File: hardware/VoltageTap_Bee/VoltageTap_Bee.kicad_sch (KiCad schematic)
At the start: 50 parts, among them J101 Conn_02x05_Odd_Even, J102 VT, J106 uart, Q101 TSM2328CX, SW101 SW_Push, U101 XMSM0G3507SDGS28R, U102 ISOM8110DFS, U103 ISO1044BD, U104 TLP176AM, U105 AP7384-50SA, U106 STISO620

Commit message: c&p master
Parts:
- removed CR?: ESD2CAN36DBZRQ1, Package_TO_SOT_SMD:TSOT-23_HandSoldering, symbol zzLocalLibrary:ESD2CAN36DBZRQ1
- removed D101, D102: LED, LED_SMD:LED_0603_1608Metric, symbol Device:LED
- removed D?: ES1D, Diode_SMD:D_SMA, symbol Device:D_Schottky_Small
- removed FL?: Choke_CommonMode_FerriteCore_1243, Inductor_SMD:L_CommonModeChoke_Coilcraft_1812CAN, symbol Filter:Choke_CommonMode_FerriteCore_1243
- removed J?: Conn_01x04_Pin, Connector_PinHeader_2.54mm:PinHeader_1x04_P2.54mm_Vertical, symbol Connector:Conn_01x04_Pin
- removed J?: HRLV, Connector_Molex:Molex_Micro-Fit_3.0_43045-0600_2x03_P3.00mm_Horizontal, symbol Connector_Generic:Conn_02x03_Top_Bottom
- removed Q101: TSM2328CX, Package_TO_SOT_SMD:SOT-23-3, symbol Transistor_FET:Q_NMOS_GSD
- removed R105, R111: 750, Resistor_SMD:R_1206_3216Metric_Pad1.30x1.75mm_HandSolder, symbol Device:R_US
- removed R107: 88.7k, Resistor_SMD:R_0805_2012Metric_Pad1.20x1.40mm_HandSolder, symbol Device:R_Small_US
- removed R112, R113, R114: 750, Resistor_SMD:R_1206_3216Metric_Pad1.30x1.75mm_HandSolder, symbol Device:R_Small_US
- removed U102: ISOM8110DFS, zzLocalLibraries-Footprints:ISOM811_SOIC-4_DFG, symbol zzLocalLibrary:ISOM811_0_3
- removed U103: ISO1044BD, Package_SO:SOIC-8_5.3x5.3mm_P1.27mm, symbol Interface_CAN_LIN:ISO1044BD
- removed U105: AP7384-50SA, Package_TO_SOT_SMD:SOT-23, symbol Regulator_Linear:AP7384-50SA
- removed U106: STISO620, Package_SO:SOIC-8_7.5x5.85mm_P1.27mm, symbol zzLocalLibrary:STISO621
- added C106: 22u, Capacitor_SMD:C_0805_2012Metric_Pad1.18x1.45mm_HandSolder, symbol Device:C_Small
- added C107, C109: 100n, Capacitor_SMD:C_0603_1608Metric_Pad1.08x0.95mm_HandSolder, symbol Device:C_Small
- added C112: 1u, Capacitor_SMD:C_0603_1608Metric_Pad1.08x0.95mm_HandSolder, symbol Device:C_Small
- added CR101: ESD2CAN36DBZRQ1, Package_TO_SOT_SMD:TSOT-23_HandSoldering, symbol zzLocalLibrary:ESD2CAN36DBZRQ1
- added D101: ES1D, Diode_SMD:D_SMA, symbol Device:D_Schottky_Small
- added D102: green, LED_SMD:LED_0805_2012Metric_Pad1.15x1.40mm_HandSolder, symbol Device:LED_Small
- added D104: yellow, LED_SMD:LED_0805_2012Metric_Pad1.15x1.40mm_HandSolder, symbol Device:LED_Small
- added FL101: Choke_CommonMode_FerriteCore_1243, Inductor_SMD:L_CommonModeChoke_Coilcraft_1812CAN, symbol Filter:Choke_CommonMode_FerriteCore_1243
- added J102: HRLV daisy A, Connector_Molex:Molex_Micro-Fit_3.0_43045-0600_2x03_P3.00mm_Horizontal, symbol Connector_Generic:Conn_02x03_Top_Bottom
- added J103: HRLV daisy B, Connector_Molex:Molex_Micro-Fit_3.0_43045-0600_2x03_P3.00mm_Horizontal, symbol Connector_Generic:Conn_02x03_Top_Bottom
- added R105: 10k, Resistor_SMD:R_0805_2012Metric_Pad1.20x1.40mm_HandSolder, symbol Device:R_Small_US
- added R109: 3.32k, Resistor_SMD:R_0805_2012Metric_Pad1.20x1.40mm_HandSolder, symbol Device:R_Small_US
- added U101: TPSM33606S5QRDNRQ1, zzLocalLibraries-Footprints:RDN0011A_TEX, symbol zzLocalLibrary:TPSM33606S5QRDNRQ1
- added U103: ISOM8110DFS, zzLocalLibraries-Footprints:ISOM811_SOIC-4_DFG, symbol zzLocalLibrary:ISOM811_0_3
- added U104: NCP163ASN330T1G, Package_TO_SOT_SMD:SOT-23-5_HandSoldering, symbol Regulator_Linear:NCP163ASN330T1G
- added U105: XISO6441DWR, zzLocalLibraries-Footprints:SOIC16_DW_TEX-M, symbol zzLocalLibrary:XISO6441DWR
- added U106: MCP2542FDxMF, Package_SO:SOIC-8_3.9x4.9mm_P1.27mm, symbol Interface_CAN_LIN:MCP2542FDxMF
- C101: value 100n -> 220n; footprint Capacitor_SMD:C_0603_1608Metric_Pad1.08x0.95mm_HandSolder -> Capacitor_SMD:C_0805_2012Metric_Pad1.18x1.45mm_HandSolder; Mouser Part Number 710-885012206095 -> (none); mouser https://www.mouser.com/ProductDetail/Wurth-Elektronik/88501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 -> https://www.mouser.com/ProductDetail/Samsung-Electro-Mechan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; specs 100nF, 10%, 50V, X7R, -55C, +125C -> 100VDC, X7R, 10%, -55C, +125C, 220nF; unit x1 0.10 -> (none); unit x10 0.029 -> 0.054; unit x100 0.017 -> (none); unit x50 0.02 -> (none)
- C102: value 100n -> 1u; Mouser Part Number 710-885012206095 -> (none); mouser https://www.mouser.com/ProductDetail/Wurth-Elektronik/88501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 -> https://www.mouser.com/ProductDetail/Samsung-Electro-Mechan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; specs 100nF, 10%, 50V, X7R, -55C, +125C -> 1uF, 25VDC, 10%, -55C, +125C; unit x1 0.10 -> 0.15; unit x10 0.029 -> 0.061; unit x100 0.017 -> (none); unit x50 0.02 -> (none)
- C104: value 1u -> 22u; footprint Capacitor_SMD:C_1206_3216Metric_Pad1.33x1.80mm_HandSolder -> Capacitor_SMD:C_0805_2012Metric_Pad1.18x1.45mm_HandSolder; Mouser Part Number 187-CL31B105KCHNNNE -> (none); mouser https://www.mouser.com/ProductDetail/Samsung-Electro-Mechanics/CL31B105KCHNNNE?qs=349EhDEZ59qH1i3RhF2lug%3D%3D -> https://www.mouser.com/ProductDetail/Samsung-Electro-Mechanics/CL21A226MAYNNNE?qs=sGAEpiMZZMsh%252B1woXyUXj9e2R%2FOkAO5o4FNiyGuFzx8%3D; specs 1uF, 100VDC, X7R, 10%, -55C, +125C -> 22uF, 25V, 20%, X5R, -55C, +85C, mlcc; unit x10 0.07 -> 0.043
- D103: value green -> blue; Mouser Part Number 743-IN-S85CS5G -> (none); mouser https://www.mouser.com/ProductDetail/Inolux/IN-S85CS5G?qs=s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 -> https://www.mouser.com/ProductDetail/Inolux/IN-S85CS5B?qs=s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; specs 5mA, 90mW, 2.5Vf, 5Vr, 525nm, 230mcd -> 5mA, 90mW, 2.6Vf, 5Vr, 470nm, 40mcd; unit x1 0.27 -> 0.22; unit x10 0.187 -> 0.15
- R108: value 88.7k -> 3.32k; Mouser Part Number 603-AC0805FR-0788K7L -> (none); mouser https://www.mouser.com/ProductDetail/YAGEO/AC0805FR-0788K7L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 -> https://www.mouser.com/ProductDetail/Walsin/WR08X3321FTL?qs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; specs 88.7kR, 125mW, 150V, 100ppm, 1%, -55C, +155C -> 3.32kOhm, 1%, 150V, 125mW, 100ppm, -55C, 155C; unit x1 0.01 -> 0.10; unit x10 0.011 -> .025
- R110: value 88.7k -> 10k; Mouser Part Number 603-AC0805FR-0788K7L -> 603-AC0805FR-7W10KL; mouser https://www.mouser.com/ProductDetail/YAGEO/AC0805FR-0788K7L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 -> https://www.mouser.com/ProductDetail/YAGEO/AC0805FR-7W10KL?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; specs 88.7kR, 125mW, 150V, 100ppm, 1%, -55C, +155C -> 10k , 250mW, 150V, 1%, 100ppm, -55C, +155C; unit x1 0.01 -> 0.1; unit x10 0.011 -> 0.015
- SW101: footprint Button_Switch_SMD:SW_SPST_PTS645Sx43SMTR92 -> zzLocalLibraries-Footprints:wurth elektronik 4.7x3.5mm side push button; Mouser Part Number 611-KSC251JSPDELTALF -> (none); mouser https://www.mouser.com/ProductDetail/CK/KSC251J-SP-DELTA-LF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 -> (none); mouser  (none) -> https://www.mouser.com/ProductDetail/Wurth-Elektronik/43633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; unit x1 (none) -> 0.58; unit x10 0.532 -> 0.541
- U102: renamed from U104; footprint Package_SO:Toshiba_SOIC-4-6_4.4x3.6mm_P1.27mm -> Package_SO:SOIC-4_4.55x3.7mm_P2.54mm
- renumbered C1 to C108, C3 to C110, C4 to C111, J102 to J101, J101 to J104, J106 to J105, R109 to R107, R1 to R111, U101 to U107
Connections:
- net IL_EN is gone; now on net IL EN: U107.11 (PA4_/_LFCLK_IN_/_LFXOUT)
- net +3.3V: now also C106.1, C107.1, U104.5 (VOUT), U105.1 (VCC1), U106.5 (VIO)
- net -BATT: now also C105.2, R105.1, U105.15 (GND2), U105.9 (GND2); no longer C101.2, C102.2, C103.2, C108.2, C110.2, C111.2, J104.3 (Pin_3), J104.5 (Pin_5), J104.7 (Pin_7), J104.9 (Pin_9), J105.1 (Pin_1), R108.1, R111.2, SW101.2, U107.8 (VSS)
- net BQ76952 1/CFETOFF: now also R102.1; no longer R103.1
- net BQ76952 1/HDQ: now also R101.1; no longer R104.1
- net BQ76952 1/RST_SHUT: now also R105.2, U103.3 (E); no longer R106.1
- net BQ76952 1/SCL: now also R103.1; no longer R102.2
- net BQ76952 1/SDA: now also R104.1; no longer R101.1
- net CAN_H: now also CR101.2 (IO), FL101.1, J102.6 (Pin_6), J103.6 (Pin_6)
- net CAN_L: now also CR101.1 (IO), FL101.4, J102.3 (Pin_3), J103.3 (Pin_3)
- net GLV+: now also D101.2 (A), J102.5 (Pin_5), J103.5 (Pin_5)
- net IL+: now also U102.4, J102.1 (Pin_1), J103.4 (Pin_4); no longer U102.6
- net IL-: now also U102.6, J102.4 (Pin_4), J103.1 (Pin_1); no longer U102.4
- net PA10_UART0-TX_XDS: now also J105.2 (Pin_2); no longer J105.3 (Pin_3)
- net PA11_UART0-RX_XDS: now also J105.3 (Pin_3); no longer J105.2 (Pin_2)
- net PA16_SPI1_MISO: now also U105.6 (OUTD); no longer R101.2
- net PA17_SPI1_SCK: now also U105.5 (INC); no longer R102.1
- net PA18_SPI1_MOSI: now also U105.3 (INA); no longer R104.2
- net PA26_CAN_TX: now also U106.1 (TXD)
- net PA27_CAN_RX: now also U106.4 (RXD)
- net PB14_BBQ_CS: now also U105.4 (INB); no longer R103.2
- net at C108.1, U107.3 (VCORE): now also C109.1; no longer C103.1
- net IL EN: now reaches R106.2
- net at U102.1: now also D102.1 (K)
- net GND: now reaches D103.1 (K), U102.3
- net GND: now also C101.2, C102.2, C103.2, C104.2, C108.2, C110.2, C111.2, J104.3 (Pin_3), J104.5 (Pin_5), J104.7 (Pin_7), J104.9 (Pin_9), J105.1 (Pin_1), R111.2, SW101.1, U107.8 (VSS), C106.2, C107.2, C109.2, C112.2, CR101.3 (GND), J102.2 (Pin_2), J103.2 (Pin_2), R109.1, U101.10 (GND), U101.11 (MODE/SYNCH), U103.2 (-TX), U104.2 (GND), U105.2 (GND1), U105.8 (GND1), U106.2 (VSS), U106.8 (STBY), U106.9 (VSS)
- net +5V: now reaches C104.1
- net +5V: now also C103.1, C112.1, D104.2 (A), U101.4 (VOUT), U101.9 (FB), U104.1 (VIN), U104.3 (EN), U106.3 (VDD)
- net at D103.2 (A): now also R108.2
- net 5v renamed BQ0_3.3v
- net BQ0_3.3v: now also U103.4 (C), U105.16 (VCC2)
- net BLINK renamed led.sched
- net led.sched: now also R108.1
- removed net GLV-: C104.2, C105.2
- net RST_N renamed MCU_RESET
- net MCU_RESET: now also SW101.2; no longer C102.1, SW101.1
- new net: R103.2, U105.12 (OUTC)
- new net: R104.2, U105.11 (IND)
- new net: C101.1, D101.1 (K), U101.2 (EN), U101.3 (VIN)
- new net: FL101.2, U106.7 (CANH)
- new net: FL101.3, U106.6 (CANL)
- new net: R102.2, U105.13 (OUTB)
- new net: R101.2, U105.14 (OUTA)
- new net: C102.1, U101.8 (VCC)
- new net: D102.2 (A), R106.1
- new net: D104.1 (K), R109.2
- new net: R107.1, U103.1 (+TX)
- no-connect marks 11 -> 17
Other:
- note added: "(HRLV)"
- note added: "CAN bus"
- note added: "HV"
- note added: "LV"
- note added: "SSR very sensitive, no need to downsize s-R"
- note added: "interlock"
- note added: "og(7/13/2025)"
- note added: "power"
- note removed: "2.1"
- note removed: "7/13/2025"
- note removed: "CAN"
- note removed: "EVAL MSPM0G3507 BQ76952"
- note removed: "Files at github.com/Gregification/BeeMS"
- note removed: "Interlock"
- note removed: "Isolated UART Connection"
- note removed: "MCU work?"
- note removed: "PS"
- note removed: "TODO: power isolators using BQ reg2, set reg2 to 3v3. required since reg1 cant supply enough power in some cases"
- note removed: "reset btn"
- moved on the sheet: C108, C110, C111, J101, R103, R104, R107, R111, TH101, TH102, TH103, TH104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

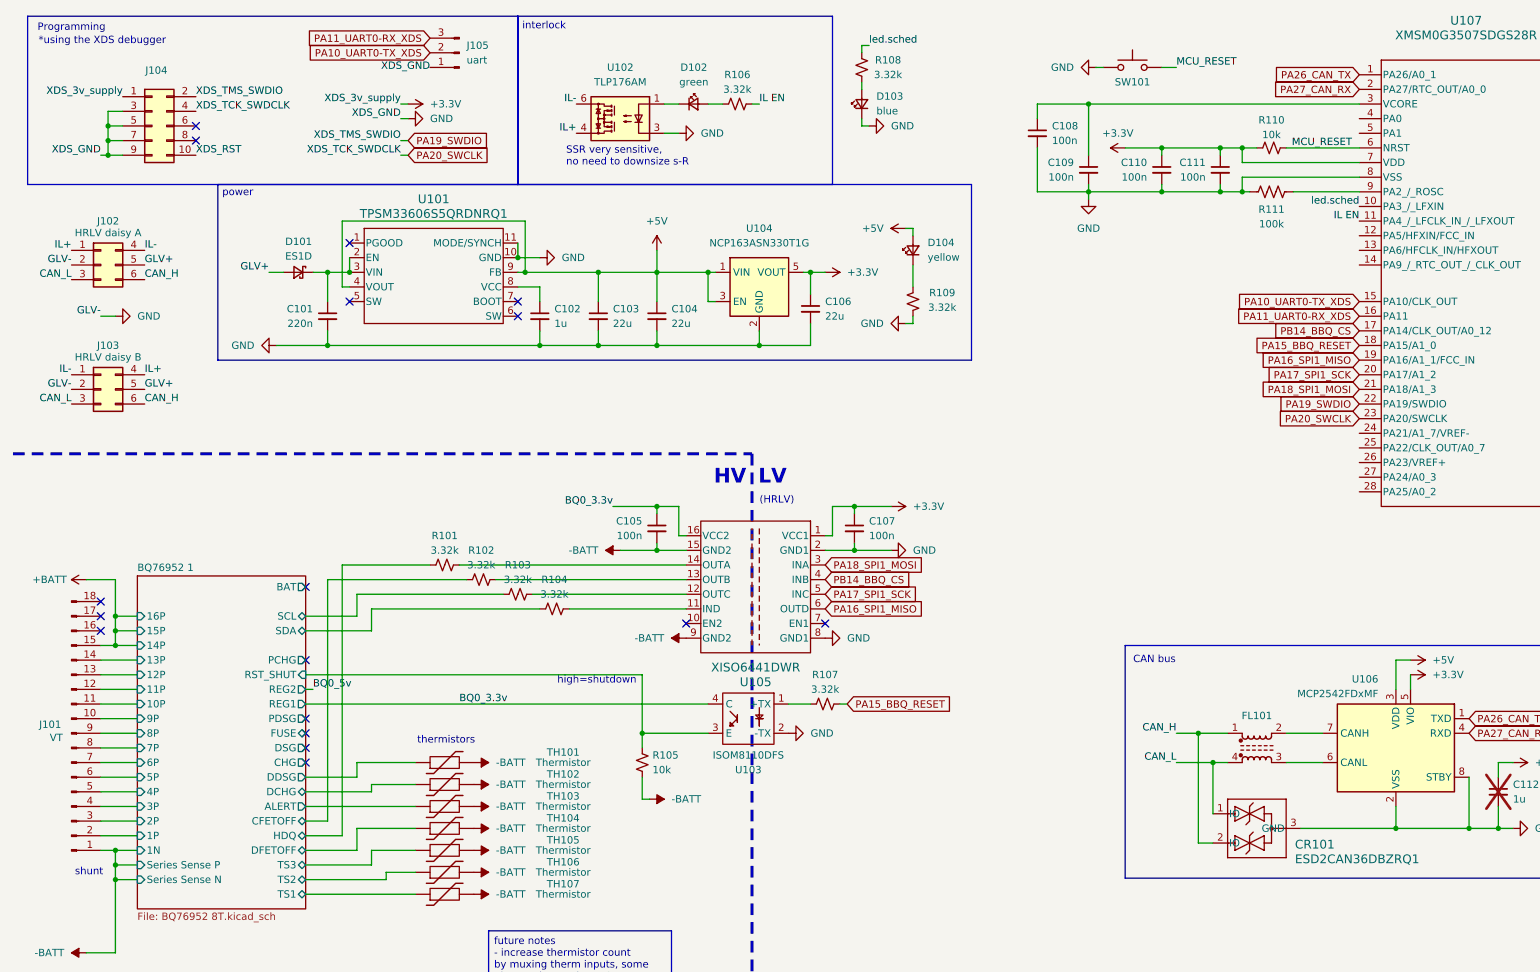
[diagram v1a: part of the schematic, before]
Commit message: layout update: cell bal and daisy pins
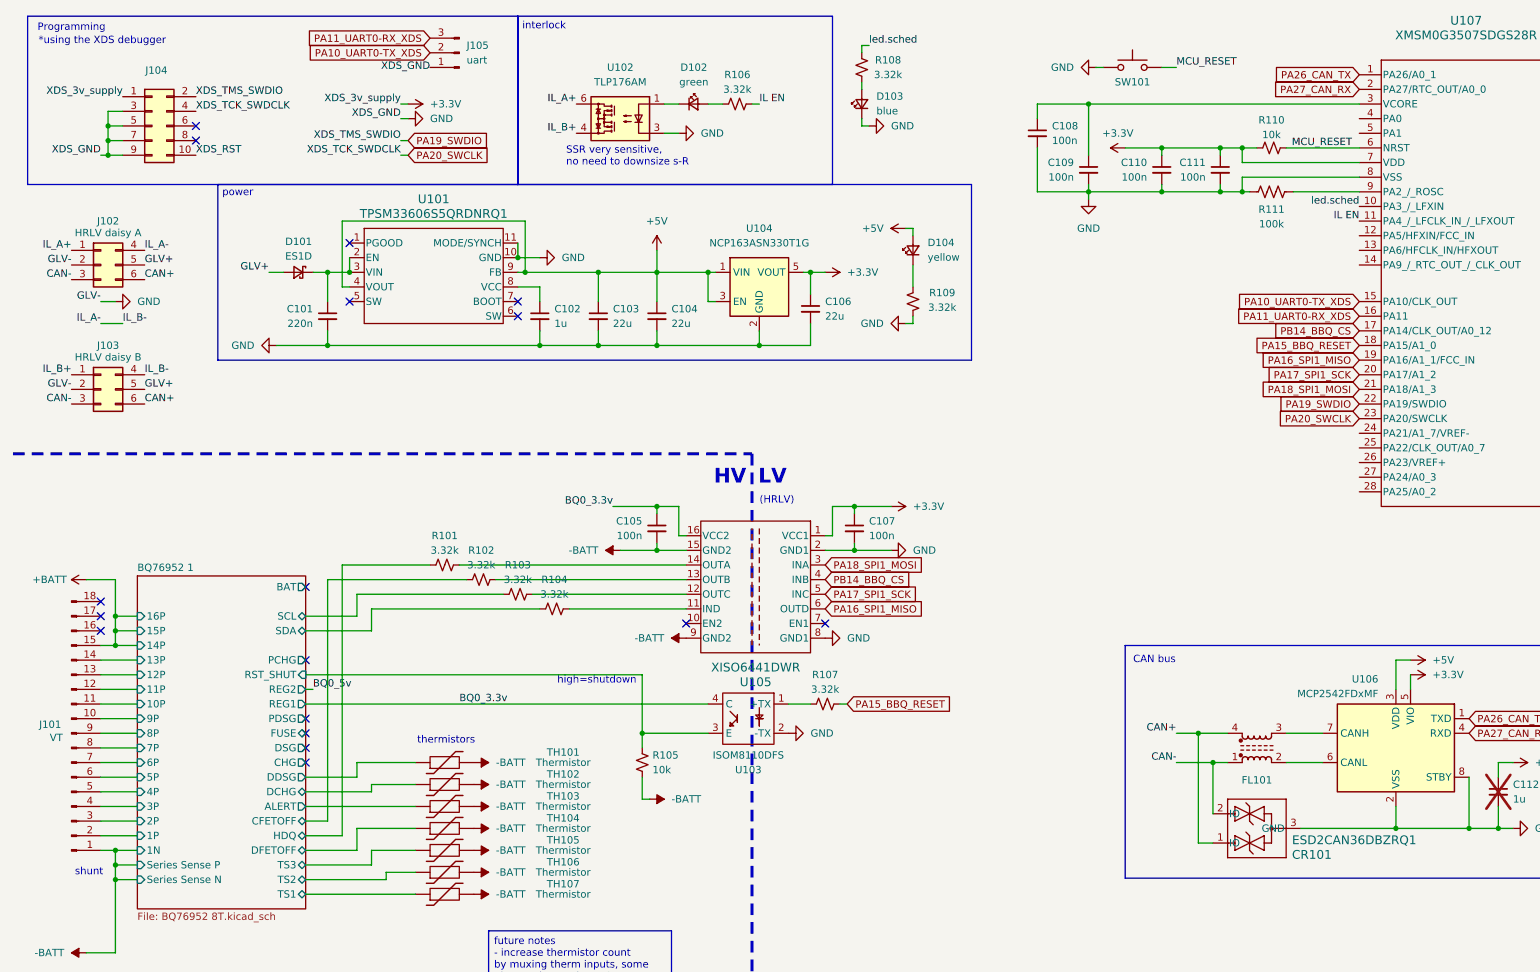
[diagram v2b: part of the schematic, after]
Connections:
- net at FL101.2: now also U106.6 (CANL); no longer U106.7 (CANH)
- net at FL101.3: now also U106.7 (CANH); no longer U106.6 (CANL)
- net CAN_H renamed CAN+
- net CAN+: now also CR101.1 (IO), FL101.4; no longer CR101.2 (IO), FL101.1
- net CAN_L renamed CAN-
- net CAN-: now also CR101.2 (IO), FL101.1; no longer CR101.1 (IO), FL101.4
- removed net IL+: J102.1 (Pin_1), J103.4 (Pin_4), U102.4
- removed net IL-: J102.4 (Pin_4), J103.1 (Pin_1), U102.6
- new net IL_A+: J102.1 (Pin_1), U102.6
- new net IL_A-: J102.4 (Pin_4), J103.4 (Pin_4)
- new net IL_B+: J103.1 (Pin_1), U102.4
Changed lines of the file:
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@@
 	(wire
 		(pts
-			(xy 26.67 67.31) (xy 29.21 67.31)
+			(xy 26.67 64.77) (xy 29.21 64.77)
 		)
 		(stroke
@@
 	(wire
 		(pts
+			(xy 26.67 68.58) (xy 30.48 68.58)
+		)
+		(stroke
+			(width 0)
+			(type default)
+		)
+	)
+	(wire
+		(pts
 			(xy 198.12 30.48) (xy 245.11 30.48)
 		)
@@
 		)
 	)
-	(label "CAN_L"
-		(at 21.59 60.96 180)
-		(effects
-			(font
-				(size 1.27 1.27)
-			)
-			(justify right bottom)
-		)
-	)
-	(label "CAN_H"
-		(at 213.36 139.7 180)
-		(effects
-			(font
-				(size 1.27 1.27)
-			)
-			(justify right bottom)
-		)
-	)
 	(label "XDS_TMS_SWDIO"
 		(at 78.74 36.83 180)
@@
 		)
 	)
+	(label "CAN-"
+		(at 21.59 60.96 180)
+		(effects
+			(font
+				(size 1.27 1.27)
+			)
+			(justify right bottom)
+		)
+	)
 	(label "BQ0_3.3v"
 		(at 115.57 100.33 180)
@@
 		)
 	)
+	(label "CAN+"
+		(at 213.36 139.7 180)
+		(effects
+			(font
+				(size 1.27 1.27)
+			)
+			(justify right bottom)
+		)
+	)
 	(label "MCU_RESET"
 		(at 243.84 38.1 180)
@@
 		)
 	)
-	(label "IL-"
-		(at 21.59 77.47 180)
+	(label "IL_B-"
+		(at 34.29 77.47 0)
 		(effects
 			(font
 				(size 1.27 1.27)
 			)
-			(justify right bottom)
+			(justify left bottom)
 		)
 	)
@@
 		)
 	)
-	(label "IL+"
+	(label "IL_A+"
 		(at 21.59 55.88 180)
 		(effects
@@
 		)
 	)
-	(label "IL-"
-		(at 109.22 30.48 180)
+	(label "XDS_GND"
+		(at 78.74 33.02 180)
 		(effects
 			(font
@@
 		)
 	)
-	(label "XDS_GND"
-		(at 78.74 33.02 180)
+	(label "CAN+"
+		(at 34.29 82.55 0)
 		(effects
 			(font
 				(size 1.27 1.27)
 			)
-			(justify right bottom)
+			(justify left bottom)
 		)
 	)
-	(label "CAN_H"
-		(at 34.29 82.55 0)
+	(label "GLV-"
+		(at 26.67 64.77 180)
 		(effects
 			(font
 				(size 1.27 1.27)
 			)
-			(justify left bottom)
+			(justify right bottom)
 		)
 	)
-	(label "GLV-"
-		(at 26.67 67.31 180)
+	(label "IL_A+"
+		(at 109.22 30.48 180)
 		(effects
 			(font
@@
 		)
 	)
-	(label "CAN_L"
+	(label "CAN-"
 		(at 21.59 82.55 180)
 		(effects
@@
 		)
 	)
-	(label "CAN_H"
-		(at 34.29 60.96 0)
+	(label "XDS_RST"
+		(at 43.18 39.37 0)
 		(effects
 			(font
@@
 		)
 	)
-	(label "XDS_RST"
-		(at 43.18 39.37 0)
+	(label "IL_B-"
+		(at 30.48 68.58 0)
 		(effects
 			(font
@@
 		)
 	)
-	(label "CAN_L"
-		(at 213.36 144.78 180)
+	(label "CAN+"
+		(at 34.29 60.96 0)
 		(effects
 			(font
 				(size 1.27 1.27)
 			)
-			(justify right bottom)
+			(justify left bottom)
 		)
 	)
@@
 		)
 	)
-	(label "IL+"
-		(at 34.29 77.47 0)
+	(label "IL_B+"
+		(at 109.22 35.56 180)
 		(effects
 			(font
 				(size 1.27 1.27)
 			)
-			(justify left bottom)
+			(justify right bottom)
+		)
+	)
+	(label "IL_B+"
+		(at 21.59 77.47 180)
+		(effects
+			(font
+				(size 1.27 1.27)
+			)
+			(justify right bottom)
 		)
 	)
@@
 		)
 	)
-	(label "IL+"
-		(at 109.22 35.56 180)
+	(label "CAN-"
+		(at 213.36 144.78 180)
 		(effects
 			(font
@@
 		)
 	)
-	(label "IL-"
+	(label "IL_A-"
 		(at 34.29 55.88 0)
 		(effects
@@
 		)
 	)
+	(label "IL_A-"
+		(at 26.67 68.58 180)
+		(effects
+			(font
+				(size 1.27 1.27)
+			)
+			(justify right bottom)
+		)
+	)
 	(global_label "PB14_BBQ_CS"
 		(shape input)
@@
 		(lib_id "Filter:Choke_CommonMode_FerriteCore_1243")
 		(at 227.33 142.24 0)
+		(mirror x)
 		(unit 1)
 		(exclude_from_sim no)
@@
 		(dnp no)
 		(property "Reference" "FL101"
-			(at 227.33 136.652 0)
+			(at 227.33 147.828 0)
 			(effects
 				(font
@@
 		)
 		(property "Value" "Choke_CommonMode_FerriteCore_1243"
-			(at 227.203 137.16 0)
+			(at 227.203 147.32 0)
 			(effects
 				(font
@@
 		)
 		(property "Footprint" "Inductor_SMD:L_CommonModeChoke_Coilcraft_1812CAN"
-			(at 227.33 148.59 0)
+			(at 227.33 135.89 0)
 			(effects
 				(font
@@
 		)
 		(property "Datasheet" "~"
-			(at 227.33 150.495 0)
+			(at 227.33 133.985 0)
 			(effects
 				(font
@@
 		)
 		(property "Description" "EMI 2-inductor common mode filter"
-			(at 231.394 143.002 0)
+			(at 231.394 141.478 0)
 			(effects
 				(font
@@
 	(symbol
 		(lib_id "power:GND")
-		(at 29.21 67.31 90)
+		(at 29.21 64.77 90)
 		(unit 1)
 		(exclude_from_sim no)
@@
 		(fields_autoplaced yes)
 		(property "Reference" "#PWR0103"
-			(at 35.56 67.31 0)
+			(at 35.56 64.77 0)
 			(effects
 				(font
@@
 		)
 		(property "Value" "GND"
-			(at 33.02 67.3099 90)
+			(at 33.02 64.7699 90)
 			(effects
 				(font
@@
 		)
 		(property "Footprint" ""
-			(at 29.21 67.31 0)
+			(at 29.21 64.77 0)
 			(effects
 				(font
@@
 		)
 		(property "Datasheet" ""
-			(at 29.21 67.31 0)
+			(at 29.21 64.77 0)
 			(effects
 				(font
@@
 		)
 		(property "Description" "Power symbol creates a global label with name \"GND\" , ground"
-			(at 29.21 67.31 0)
+			(at 29.21 64.77 0)
 			(effects
 				(font
@@
 		(lib_id "zzLocalLibrary:ESD2CAN36DBZRQ1")
 		(at 227.33 156.21 0)
+		(mirror x)
 		(unit 1)
 		(exclude_from_sim no)
@@
 		(dnp no)
 		(property "Reference" "CR101"
-			(at 233.934 159.004 0)
+			(at 233.426 160.782 0)
 			(effects
 				(font
@@
 		)
 		(property "Value" "ESD2CAN36DBZRQ1"
-			(at 233.934 161.544 0)
+			(at 233.426 158.242 0)
 			(effects
 				(font

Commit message: bee
wee
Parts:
- TH101, TH102, TH103, TH104, TH105, TH106: now not fitted; now left out of the parts list
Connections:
- net BQ76952 1/CFETOFF: now also R101.1; no longer R102.1
- net BQ76952 1/HDQ: now also R102.1; no longer R101.1
- net IL EN: now also U107.28 (PA25/A0_2); no longer U107.11 (PA4_/_LFCLK_IN_/_LFXOUT)
- net PA18_SPI1_MOSI: now also U105.4 (INB); no longer U105.3 (INA)
- net led.sched: now also U107.14 (PA9_/_RTC_OUT_/_CLK_OUT); no longer U107.10 (PA3_/_LFXIN)
- net bbqCS: now reaches U107.24 (PA21/A1_7/VREF-)
- net bbqCS: now also U105.3 (INA)
- net bbqrst: now reaches U107.27 (PA24/A0_3)
- net bbqrst: now also R107.2
- net PA15_BBQ_RESET: no longer names the net of U107.18 (PA15/A1_0)
- net PA15_BBQ_RESET: no longer R107.2
- net PB14_BBQ_CS: no longer names the net of U107.17 (PA14/CLK_OUT/A0_12)
- net PB14_BBQ_CS: no longer U105.4 (INB)
- no-connect marks 17 -> 27
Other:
- moved on the sheet: C108

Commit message: ordered
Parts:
- SW101: mouser (none) -> https://www.mouser.com/ProductDetail/Wurth-Elektronik/43435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
